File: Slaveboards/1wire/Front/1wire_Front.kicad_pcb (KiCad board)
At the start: 2 copper layers, 71.5 x 24 mm, 2 parts

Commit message: Improve libraries
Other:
- outline, holes or cut-outs redrawn
- board text added: "JLCJLCJLCJLC"

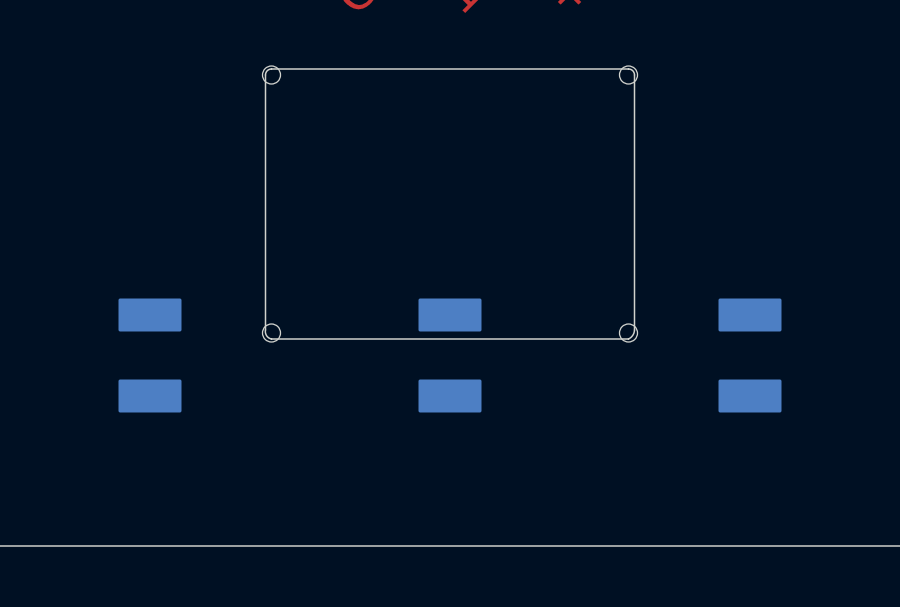
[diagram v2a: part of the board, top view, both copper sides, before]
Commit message: Remove pads from cutouts
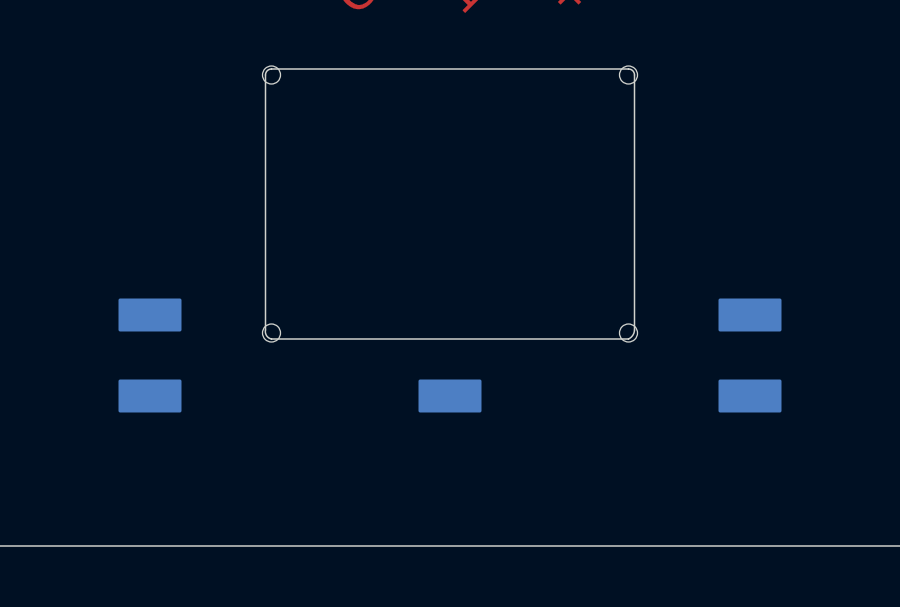
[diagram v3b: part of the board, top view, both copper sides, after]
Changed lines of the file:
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@@
-		)
-		(fp_rect
-			(start -1 -8.2)
-			(end 1 -7.2)
-			(stroke
-				(width 0.1)
-				(type solid)
-			)
-			(fill yes)
-			(layer "B.Cu")
 		)
 		(fp_rect
@@
 		)
 		(fp_rect
-			(start -1 -8.2)
+			(start -1 -5.6)
 			(end 1 -4.5)
 			(stroke

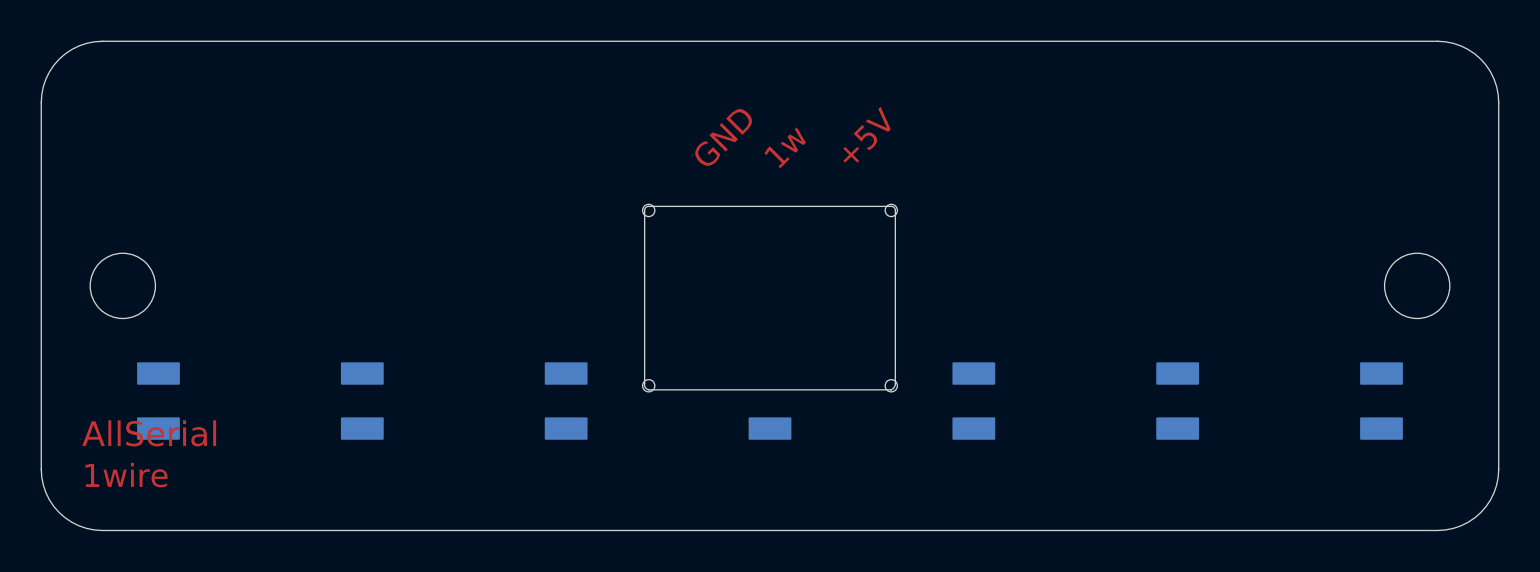
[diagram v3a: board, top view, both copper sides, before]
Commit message: Add python testskript
Add mainboard tester
Add libraries
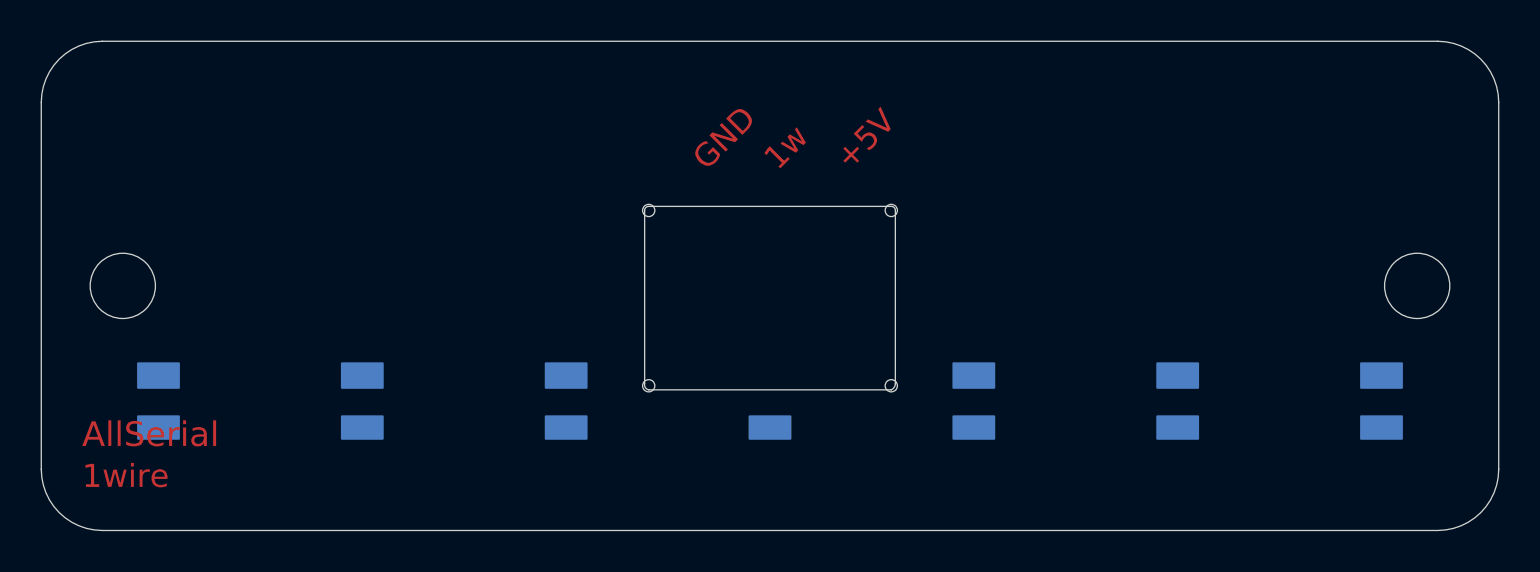
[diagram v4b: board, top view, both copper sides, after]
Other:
- board text added: "AllSerial 1wire 26/23"
- board text removed: "AllSerial 1wire front 26/23"
- board text removed: "JLCJLCJLCJLC"
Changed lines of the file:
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@@
 		(fp_rect
 			(start -31 -8.2)
-			(end -29 -7.2)
+			(end -29 -7)
 			(stroke
 				(width 0.1)
@@
 		)
 		(fp_rect
-			(start -31 -5.5)
+			(start -31 -5.6)
 			(end -29 -4.5)
 			(stroke
@@
 		(fp_rect
 			(start -21 -8.2)
-			(end -19 -7.2)
+			(end -19 -7)
 			(stroke
 				(width 0.1)
@@
 		)
 		(fp_rect
-			(start -21 -5.5)
+			(start -21 -5.6)
 			(end -19 -4.5)
 			(stroke
@@
 		(fp_rect
 			(start -11 -8.2)
-			(end -9 -7.2)
+			(end -9 -7)
 			(stroke
 				(width 0.1)
@@
 		)
 		(fp_rect
-			(start -11 -5.5)
+			(start -11 -5.6)
 			(end -9 -4.5)
 			(stroke
@@
 		)
 		(fp_rect
-			(start -1 -5.5)
+			(start -1 -5.6)
 			(end 1 -4.5)
 			(stroke
@@
 		(fp_rect
 			(start 9 -8.2)
-			(end 11 -7.2)
+			(end 11 -7)
 			(stroke
 				(width 0.1)
@@
 		)
 		(fp_rect
-			(start 9 -5.5)
+			(start 9 -5.6)
 			(end 11 -4.5)
 			(stroke
@@
 		(fp_rect
 			(start 19 -8.2)
-			(end 21 -7.2)
+			(end 21 -7)
 			(stroke
 				(width 0.1)
@@
 		)
 		(fp_rect
-			(start 19 -5.5)
+			(start 19 -5.6)
 			(end 21 -4.5)
 			(stroke
@@
 		(fp_rect
 			(start 29 -8.2)
-			(end 31 -7.2)
+			(end 31 -7)
 			(stroke
 				(width 0.1)
@@
 		)
 		(fp_rect
-			(start 29 -5.5)
+			(start 29 -5.6)
 			(end 31 -4.5)
 			(stroke
@@
 		)
 		(fp_rect
-			(start -1 -5.6)
+			(start -1 -8.2)
 			(end 1 -4.5)
 			(stroke
@@
 		)
 	)
-	(gr_text "AllSerial 1wire front 26/23"
-		(at 164.6301 98.0806 0)
+	(gr_text "AllSerial 1wire 26/23"
+		(at 148.5011 98.8426 0)
 		(layer "B.SilkS")
 		(effects
@@
 				(thickness 0.14224)
 			)
-			(justify left bottom mirror)
-		)
-	)
-	(gr_text "JLCJLCJLCJLC"
-		(at 153.2011 114.9036 0)
-		(layer "B.SilkS")
-		(effects
-			(font
-				(size 1 1)
-				(thickness 0.1)
-			)
-			(justify left bottom mirror)
+			(justify bottom mirror)
 		)
 	)
